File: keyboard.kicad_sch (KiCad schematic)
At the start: 129 parts, among them U1 MOUDLE-SEEEDUINO-XIAO

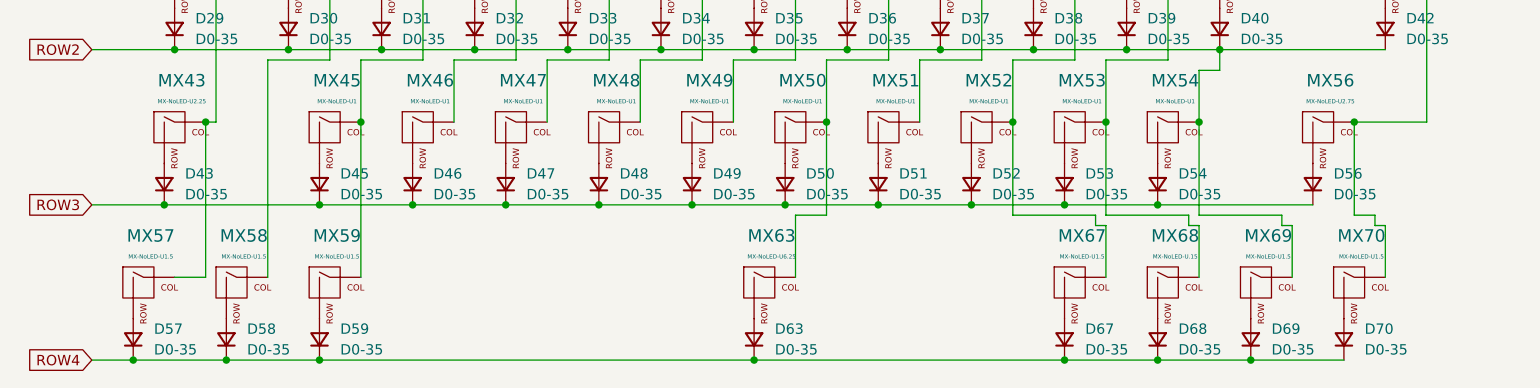
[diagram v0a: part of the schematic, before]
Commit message: Matrix placed
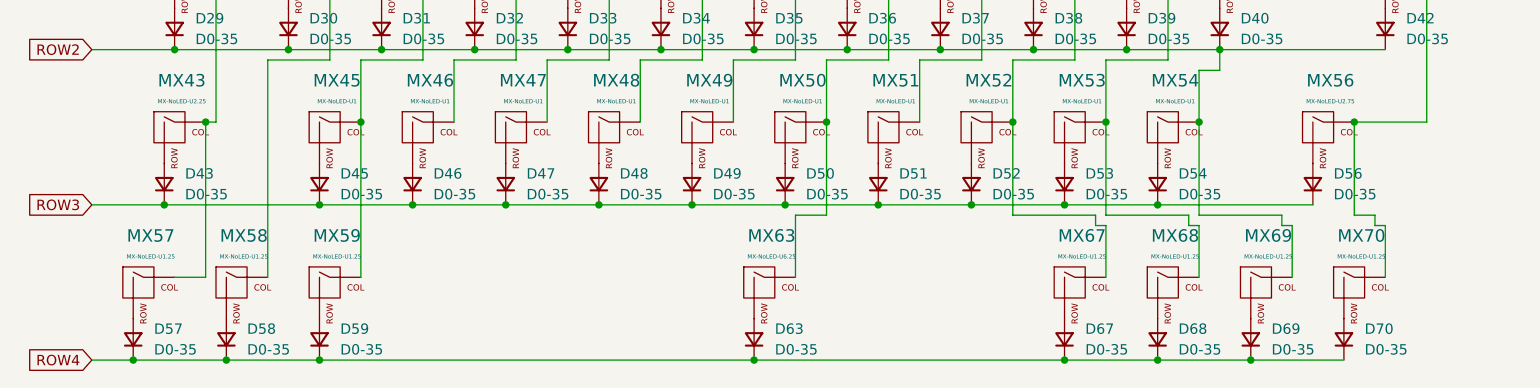
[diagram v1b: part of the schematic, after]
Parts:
- MX57, MX58, MX59, MX67, MX69, MX70: value MX-NoLED-U1.5 -> MX-NoLED-U1.25; footprint MX_Alps_Hybrid:MX-1.5U-NoLED -> MX_Alps_Hybrid:MX-1.25U-NoLED
- MX63: footprint MX_Alps_Hybrid:MX-6.5U-ReversedStabilizers-NoLED -> MX_Alps_Hybrid:MX-6.25U-ReversedStabilizers-NoLED
- MX68: value MX-NoLED-U.15 -> MX-NoLED-U1.25; footprint MX_Alps_Hybrid:MX-1.5U-NoLED -> MX_Alps_Hybrid:MX-1.25U-NoLED
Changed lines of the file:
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@@
       (effects (font (size 1.524 1.524)))
     )
-    (property "Value" "MX-NoLED-U1.5" (at 201.5432 157.48 0)
-      (effects (font (size 0.508 0.508)))
-    )
-    (property "Footprint" "MX_Alps_Hybrid:MX-1.5U-NoLED" (at 184.785 161.925 0)
+    (property "Value" "MX-NoLED-U1.25" (at 201.5432 157.48 0)
+      (effects (font (size 0.508 0.508)))
+    )
+    (property "Footprint" "MX_Alps_Hybrid:MX-1.25U-NoLED" (at 184.785 161.925 0)
       (effects (font (size 1.524 1.524)) hide)
     )
@@
       (effects (font (size 1.524 1.524)))
     )
-    (property "Value" "MX-NoLED-U1.5" (at 167.2532 157.48 0)
-      (effects (font (size 0.508 0.508)))
-    )
-    (property "Footprint" "MX_Alps_Hybrid:MX-1.5U-NoLED" (at 150.495 161.925 0)
+    (property "Value" "MX-NoLED-U1.25" (at 167.2532 157.48 0)
+      (effects (font (size 0.508 0.508)))
+    )
+    (property "Footprint" "MX_Alps_Hybrid:MX-1.25U-NoLED" (at 150.495 161.925 0)
       (effects (font (size 1.524 1.524)) hide)
     )
@@
       (effects (font (size 0.508 0.508)))
     )
-    (property "Footprint" "MX_Alps_Hybrid:MX-6.5U-ReversedStabilizers-NoLED" (at 112.395 161.925 0)
+    (property "Footprint" "MX_Alps_Hybrid:MX-6.25U-ReversedStabilizers-NoLED" (at 112.395 161.925 0)
       (effects (font (size 1.524 1.524)) hide)
     )
@@
       (effects (font (size 1.524 1.524)))
     )
-    (property "Value" "MX-NoLED-U.15" (at 178.6832 157.48 0)
-      (effects (font (size 0.508 0.508)))
-    )
-    (property "Footprint" "MX_Alps_Hybrid:MX-1.5U-NoLED" (at 161.925 161.925 0)
+    (property "Value" "MX-NoLED-U1.25" (at 178.6832 157.48 0)
+      (effects (font (size 0.508 0.508)))
+    )
+    (property "Footprint" "MX_Alps_Hybrid:MX-1.25U-NoLED" (at 161.925 161.925 0)
       (effects (font (size 1.524 1.524)) hide)
     )
@@
       (effects (font (size 1.524 1.524)))
     )
-    (property "Value" "MX-NoLED-U1.5" (at 190.1132 157.48 0)
-      (effects (font (size 0.508 0.508)))
-    )
-    (property "Footprint" "MX_Alps_Hybrid:MX-1.5U-NoLED" (at 173.355 161.925 0)
+    (property "Value" "MX-NoLED-U1.25" (at 190.1132 157.48 0)
+      (effects (font (size 0.508 0.508)))
+    )
+    (property "Footprint" "MX_Alps_Hybrid:MX-1.25U-NoLED" (at 173.355 161.925 0)
       (effects (font (size 1.524 1.524)) hide)
     )
@@
       (effects (font (size 1.524 1.524)))
     )
-    (property "Value" "MX-NoLED-U1.5" (at 75.8132 157.48 0)
-      (effects (font (size 0.508 0.508)))
-    )
-    (property "Footprint" "MX_Alps_Hybrid:MX-1.5U-NoLED" (at 59.055 161.925 0)
+    (property "Value" "MX-NoLED-U1.25" (at 75.8132 157.48 0)
+      (effects (font (size 0.508 0.508)))
+    )
+    (property "Footprint" "MX_Alps_Hybrid:MX-1.25U-NoLED" (at 59.055 161.925 0)
       (effects (font (size 1.524 1.524)) hide)
     )
@@
       (effects (font (size 1.524 1.524)))
     )
-    (property "Value" "MX-NoLED-U1.5" (at 64.3832 157.48 0)
-      (effects (font (size 0.508 0.508)))
-    )
-    (property "Footprint" "MX_Alps_Hybrid:MX-1.5U-NoLED" (at 47.625 161.925 0)
+    (property "Value" "MX-NoLED-U1.25" (at 64.3832 157.48 0)
+      (effects (font (size 0.508 0.508)))
+    )
+    (property "Footprint" "MX_Alps_Hybrid:MX-1.25U-NoLED" (at 47.625 161.925 0)
       (effects (font (size 1.524 1.524)) hide)
     )
@@
       (effects (font (size 1.524 1.524)))
     )
-    (property "Value" "MX-NoLED-U1.5" (at 52.9532 157.48 0)
-      (effects (font (size 0.508 0.508)))
-    )
-    (property "Footprint" "MX_Alps_Hybrid:MX-1.5U-NoLED" (at 36.195 161.925 0)
-      (effects (font (size 1.524 1.524)) hide)
-    )
+    (property "Value" "MX-NoLED-U1.25" (at 52.9532 157.48 0)
+      (effects (font (size 0.508 0.508)))
+    )
+    (property "Footprint" "MX_Alps_Hybrid:MX-1.25U-NoLED" (at 36.195 161.925 0)
+      (effects (font (size 1.524 1.524)) hide)
+    )

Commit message: Got everything placed
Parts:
- removed D41, D44: D0-35, onesemi-1N914:ON_Semiconductor-017AG-08_2016-O-MFG, symbol Device:D_Small
- removed D55: DO-35, onesemi-1N914:ON_Semiconductor-017AG-08_2016-O-MFG, symbol Device:D_Small
- removed U1: MOUDLE-SEEEDUINO-XIAO, XIAO_PCB:MOUDLE14P-2.54-21X17.8MM, symbol MOUDLE-SEEEDUINO-XIAO:MOUDLE-SEEEDUINO-XIAO
- added D62: DO-35, onesemi-1N914:ON_Semiconductor-017AG-08_2016-O-MFG, symbol Device:D_Small
- added D63, D64: D0-35, onesemi-1N914:ON_Semiconductor-017AG-08_2016-O-MFG, symbol Device:D_Small
- added U1: Pico, MCU_RaspberryPi_and_Boards:RPi_Pico_SMD_TH, symbol MCU_RaspberryPi_and_Boards:Pico
- D1: value D0-35 -> PI Pico
- renumbered D17 to D10, D30 to D11, D45 to D12, D59 to D13, D4 to D14, D18 to D15, D31 to D16, D46 to D17, D5 to D18, D15 to D2, D32 to D20, D47 to D21, D6 to D22, D20 to D23, D33 to D24, D48 to D25, D7 to D26, D21 to D27, D34 to D28, D49 to D29, D29 to D3, D8 to D30, D22 to D31, D35 to D32, D50 to D33, D63 to D34, D9 to D35, D23 to D36, D36 to D37, D51 to D38, D10 to D39, D43 to D4, D24 to D40, D37 to D41, D52 to D42, D11 to D43, D25 to D44, D38 to D45, D53 to D46, D67 to D47, D12 to D48, D26 to D49, D57 to D5, D39 to D50, D54 to D51, D68 to D52, D13 to D53, D27 to D54, D40 to D55, D69 to D56, D14 to D57, D28 to D58, D42 to D59, D2 to D6, D56 to D60, D70 to D61, D16 to D7, D58 to D8, D3 to D9, ENC3 to ENC1, ENC1 to ENC3, MX42 to MX41, MX43 to MX42, MX45 to MX43, MX46 to MX44, MX47 to MX45, MX48 to MX46, MX49 to MX47, MX50 to MX48, MX51 to MX49, MX52 to MX50, MX53 to MX51, MX54 to MX52, MX56 to MX53, MX57 to MX54, MX58 to MX55, MX59 to MX56, MX63 to MX57, MX67 to MX58, MX68 to MX59, MX69 to MX60, MX70 to MX61
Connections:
- net COL1: no longer MX30.1 (COL)
- net COL10: now also MX51.1 (COL); no longer ENC1.1, MX50.1 (COL)
- net COL11: now also ENC1.1, MX52.1 (COL); no longer MX51.1 (COL)
- net COL12: now also MX40.1 (COL), MX60.1 (COL)
- net COL2: now also MX30.1 (COL), MX43.1 (COL)
- net COL5: now also MX46.1 (COL); no longer MX45.1 (COL)
- net COL6: now also MX47.1 (COL); no longer MX46.1 (COL)
- net COL7: now also MX48.1 (COL), MX57.1 (COL); no longer MX47.1 (COL)
- net COL8: now also MX49.1 (COL); no longer MX48.1 (COL), MX57.1 (COL)
- net COL9: now also MX50.1 (COL); no longer MX49.1 (COL)
- net COl3: now also MX44.1 (COL); no longer MX43.1 (COL)
- net COl4: now also MX45.1 (COL); no longer MX44.1 (COL)
- net ROW0: now also D62.1 (K), D63.1 (K), D64.1 (K)
- net ROW1: no longer MX40.1 (COL)
- net ROW2: no longer D11.1 (K), D16.1 (K), D20.1 (K), D24.1 (K), D28.1 (K), D32.1 (K), D37.1 (K), D41.1 (K), D45.1 (K), D50.1 (K), D55.1 (K), D59.1 (K), MX52.1 (COL), MX60.1 (COL)
- net at ENC2.2: now also D63.2 (A)
- net at ENC3.2: now also D64.2 (A)
- net at ENC1.2: now also D62.2 (A)
- new net: D11.1 (K), D16.1 (K), D20.1 (K), D24.1 (K), D28.1 (K), D32.1 (K), D37.1 (K), D41.1 (K), D45.1 (K), D50.1 (K), D55.1 (K), D59.1 (K)
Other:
- moved on the sheet: D10, D11, D13, D15, D16, D19, D2, D20, D23, D24, D27, D28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

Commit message: Routed diodes to switches
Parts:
- renumbered D14 to D13, D15 to D14, D16 to D15, D17 to D16, D13 to D17

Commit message: Tracing mostly done just do DRC
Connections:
- net ROW0: now also U1.34 (GPIO28_ADC2)
- net ROW1: now also U1.7 (GPIO5)
- net ROW2: now also D11.1 (K), D15.1 (K), D20.1 (K), D24.1 (K), D28.1 (K), D32.1 (K), D37.1 (K), D41.1 (K), D45.1 (K), D50.1 (K), D55.1 (K), D59.1 (K), U1.6 (GPIO4)
- net ROW3: now also U1.5 (GPIO3)
- net ROW4: now also U1.4 (GPIO2)
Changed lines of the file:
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@@
   (junction (at 161.29 93.98) (diameter 0) (color 0 0 0 0)
   )
+  (junction (at 50.8 132.08) (diameter 0) (color 0 0 0 0)
+  )
   (junction (at 193.04 121.92) (diameter 0) (color 0 0 0 0)
   )
@@
   (junction (at 147.32 121.92) (diameter 0) (color 0 0 0 0)
   )
+  (junction (at 73.66 132.08) (diameter 0) (color 0 0 0 0)
+  )
   (junction (at 67.31 83.82) (diameter 0) (color 0 0 0 0)
   )
@@
   )
   (wire (pts (xy 90.17 140.97) (xy 90.17 160.02))
+    (stroke (width 0) (type default))
+  )
+  (wire (pts (xy 50.8 132.08) (xy 73.66 132.08))
     (stroke (width 0) (type default))
   )
@@
     )
   )
+  (global_label "ROW2" (shape input) (at 71.12 27.94 180) (fields_autoplaced)
+    (effects (font (size 1.27 1.27)) (justify right))
+    (property "Intersheetrefs" "${INTERSHEET_REFS}" (at 62.9528 27.94 0)
+      (effects (font (size 1.27 1.27)) (justify right) hide)
+    )
+  )
+  (global_label "ROW4" (shape input) (at 71.12 22.86 180) (fields_autoplaced)
+    (effects (font (size 1.27 1.27)) (justify right))
+    (property "Intersheetrefs" "${INTERSHEET_REFS}" (at 62.9528 22.86 0)
+      (effects (font (size 1.27 1.27)) (justify right) hide)
+    )
+  )
   (global_label "COL12" (shape input) (at 193.04 71.12 90) (fields_autoplaced)
     (effects (font (size 1.27 1.27)) (justify left))
     (property "Intersheetrefs" "${INTERSHEET_REFS}" (at 193.04 62.1666 90)
+      (effects (font (size 1.27 1.27)) (justify left) hide)
+    )
+  )
+  (global_label "ROW0" (shape input) (at 106.68 30.48 0) (fields_autoplaced)
+    (effects (font (size 1.27 1.27)) (justify left))
+    (property "Intersheetrefs" "${INTERSHEET_REFS}" (at 114.8472 30.48 0)
       (effects (font (size 1.27 1.27)) (justify left) hide)
     )
@@
     )
   )
+  (global_label "ROW1" (shape input) (at 71.12 30.48 180) (fields_autoplaced)
+    (effects (font (size 1.27 1.27)) (justify right))
+    (property "Intersheetrefs" "${INTERSHEET_REFS}" (at 62.9528 30.48 0)
+      (effects (font (size 1.27 1.27)) (justify right) hide)
+    )
+  )
   (global_label "ROW2" (shape input) (at 45.72 132.08 180) (fields_autoplaced)
     (effects (font (size 1.27 1.27)) (justify right))
@@
       (effects (font (size 1.27 1.27)) (justify right) hide)
     )
+  )
+  (global_label "ROW3" (shape input) (at 71.12 25.4 180) (fields_autoplaced)
+    (effects (font (size 1.27 1.27)) (justify right))
+    (property "Intersheetrefs" "${INTERSHEET_REFS}" (at 62.9528 25.4 0)
+      (effects (font (size 1.27 1.27)) (justify right) hide)
+    )

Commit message: Should be completely done
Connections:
- net COl3 is gone; now on net COL3: MX18.1 (COL), MX31.1 (COL), MX4.1 (COL), MX44.1 (COL), MX56.1 (COL)
- net COl4 is gone; now on net COL4: MX19.1 (COL), MX32.1 (COL), MX45.1 (COL), MX5.1 (COL)
- net COL0: now also U1.31 (GPIO26_ADC0)
- net COL1: now also U1.29 (GPIO22)
- net COL10: now also U1.16 (GPIO12)
- net COL11: now also U1.17 (GPIO13)
- net COL12: now also U1.19 (GPIO14)
- net COL13: now also U1.20 (GPIO15)
- net COL2: now also U1.21 (GPIO16)
- net COL5: now also U1.25 (GPIO19)
- net COL6: now also U1.26 (GPIO20)
- net COL7: now also U1.27 (GPIO21)
- net COL8: now also U1.14 (GPIO10)
- net COL9: now also U1.15 (GPIO11)
- net ENC2A: now reaches ENC2.A (CHANNEL_A)
- net ENC2A: now also U1.10 (GPIO7)
- net ENC2B: now reaches ENC2.B (CHANNEL_B)
- net ENC2B: now also U1.9 (GPIO6)
- net GND: now reaches ENC2.C (COMMON)
- net GND: now also ENC1.C (COMMON), ENC3.C (COMMON), U1.18 (GND)
- net ENC3B: now reaches U1.1 (GPIO0)
- net ENC3B: now also ENC3.B (CHANNEL_B)
- net ENC1B: now reaches U1.11 (GPIO8)
- net ENC1B: now also ENC1.B (CHANNEL_B)
- net ENC1A: now reaches U1.12 (GPIO9)
- net ENC1A: now also ENC1.A (CHANNEL_A)
- net ENC3A: now reaches U1.2 (GPIO1)
- net ENC3A: now also ENC3.A (CHANNEL_A)
- net COL3: now reaches U1.22 (GPIO17)
- net COL4: now reaches U1.24 (GPIO18)
- no-connect marks 0 -> 7

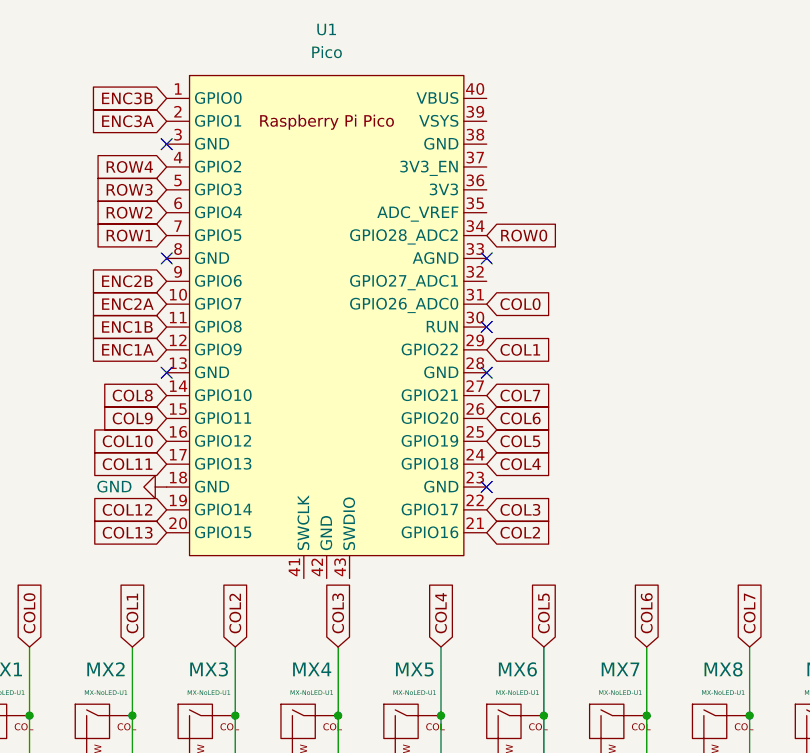
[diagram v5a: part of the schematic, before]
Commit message: With brakeouts
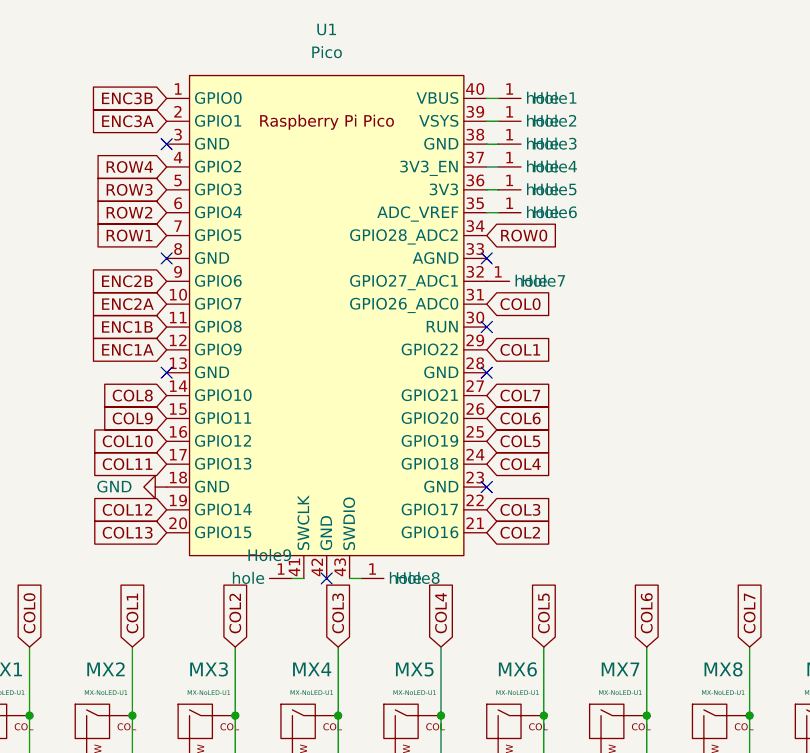
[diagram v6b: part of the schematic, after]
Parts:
- added Hole1, Hole2, Hole3, Hole4, Hole5, Hole6, Hole7, Hole8, Hole9: ~, MountingHoles:Holes, symbol My-bullshit:Hole
- ENC1, ENC2, ENC3: footprint Bourns-PEC11L-4120K-S0020:Bourns-PEC11L-4120K-S0020-MFG -> Bourns-PEC11L-4120K-S0020-*
- U1: footprint MCU_RaspberryPi_and_Boards:RPi_Pico_SMD_TH -> RPi_Pico:RPi_Pico_SMD_TH
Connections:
- net at U1.32 (GPIO27_ADC1): now also Hole7.1 (hole)
- net at U1.35 (ADC_VREF): now also Hole6.1 (hole)
- net at U1.36 (3V3): now also Hole5.1 (hole)
- net at U1.37 (3V3_EN): now also Hole4.1 (hole)
- net at U1.38 (GND): now also Hole3.1 (hole)
- net at U1.39 (VSYS): now also Hole2.1 (hole)
- net at U1.40 (VBUS): now also Hole1.1 (hole)
- net at U1.41 (SWCLK): now also Hole9.1 (hole)
- net at U1.43 (SWDIO): now also Hole8.1 (hole)
- no-connect marks 7 -> 8

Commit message: Remove brakouts
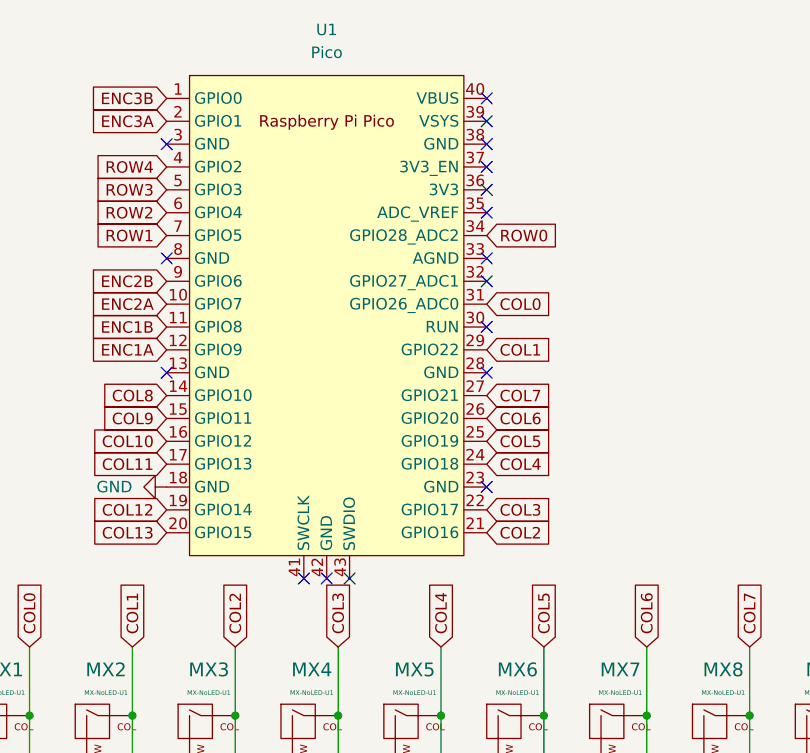
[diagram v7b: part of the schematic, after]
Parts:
- removed Hole1, Hole2, Hole3, Hole4, Hole5, Hole6, Hole7, Hole8, Hole9: ~, MountingHoles:Holes, symbol My-bullshit:Hole
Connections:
- no-connect marks 8 -> 17
